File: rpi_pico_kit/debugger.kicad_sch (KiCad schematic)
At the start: 44 parts, among them J3 USB_B, U11 74HC14, U2 RP2040, U3 NCP1117-3.3_SOT223, U4 W25Q16JVSSIQ, Y1 12MHz

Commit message: added MPNs
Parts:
- LED4: Manufacturer Part Number (none) -> LTST-C170KFKT; Supplier (none) -> Digikey; Supplier Part URL (none) -> https://www.digikey.cz/en/products/detail/lite-on-inc/LTST-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
- U3: Manufacturer Part Number (none) -> NCP1117ST33T3G; Supplier (none) -> Digikey; Supplier Part URL (none) -> https://www.digikey.cz/en/products/detail/onsemi/NCP1117ST3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
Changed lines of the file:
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@@
+      (effects (font (size 1.27 1.27)) hide)
+    )
+    (property "Manufacturer Part Number" "NCP1117ST33T3G" (id 4) (at 242.57 40.64 0)
+      (effects (font (size 1.27 1.27)) hide)
+    )
+    (property "Supplier" "Digikey" (id 5) (at 242.57 40.64 0)
+      (effects (font (size 1.27 1.27)) hide)
+    )
+    (property "Supplier Part URL" "https://www.digikey.cz/en/products/detail/onsemi/NCP1117ST33T3G/1749063" (id 6) (at 242.57 40.64 0)
       (effects (font (size 1.27 1.27)) hide)
     )
@@
       (effects (font (size 1.27 1.27)) hide)
     )
+    (property "Manufacturer Part Number" "LTST-C170KFKT" (id 4) (at 265.43 142.24 0)
+      (effects (font (size 1.27 1.27)) hide)
+    )
+    (property "Supplier" "Digikey" (id 5) (at 265.43 142.24 0)
+      (effects (font (size 1.27 1.27)) hide)
+    )
+    (property "Supplier Part URL" "https://www.digikey.cz/en/products/detail/lite-on-inc/LTST-C170KFKT/386775" (id 6) (at 265.43 142.24 0)
+      (effects (font (size 1.27 1.27)) hide)
+    )

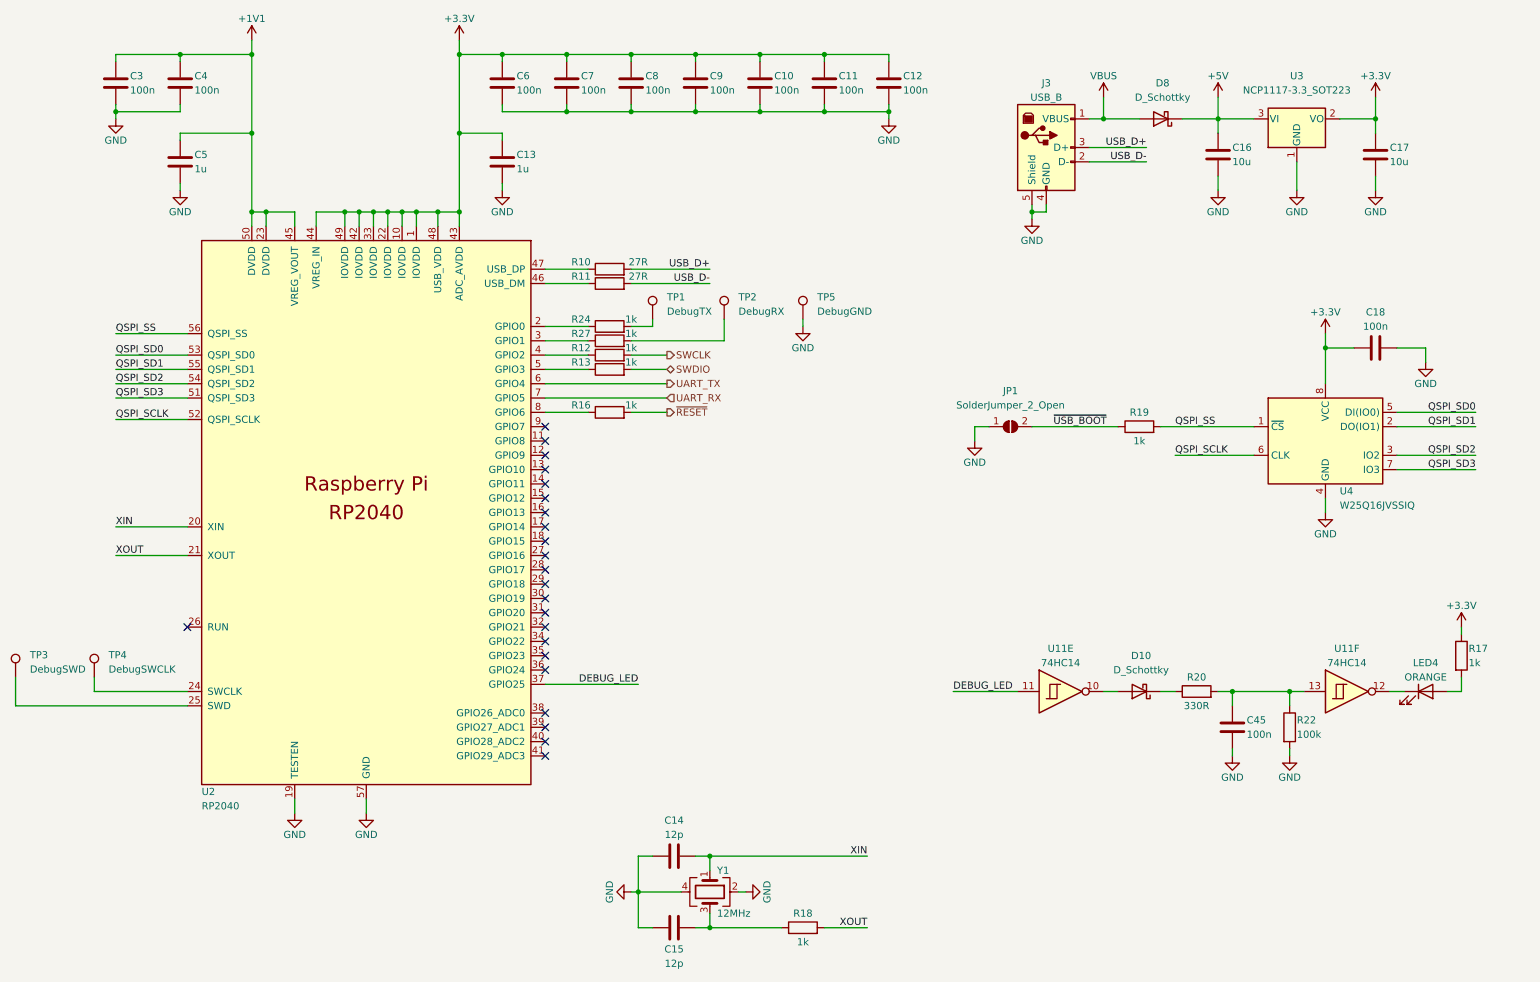
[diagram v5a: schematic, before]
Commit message: changed numbering of parts
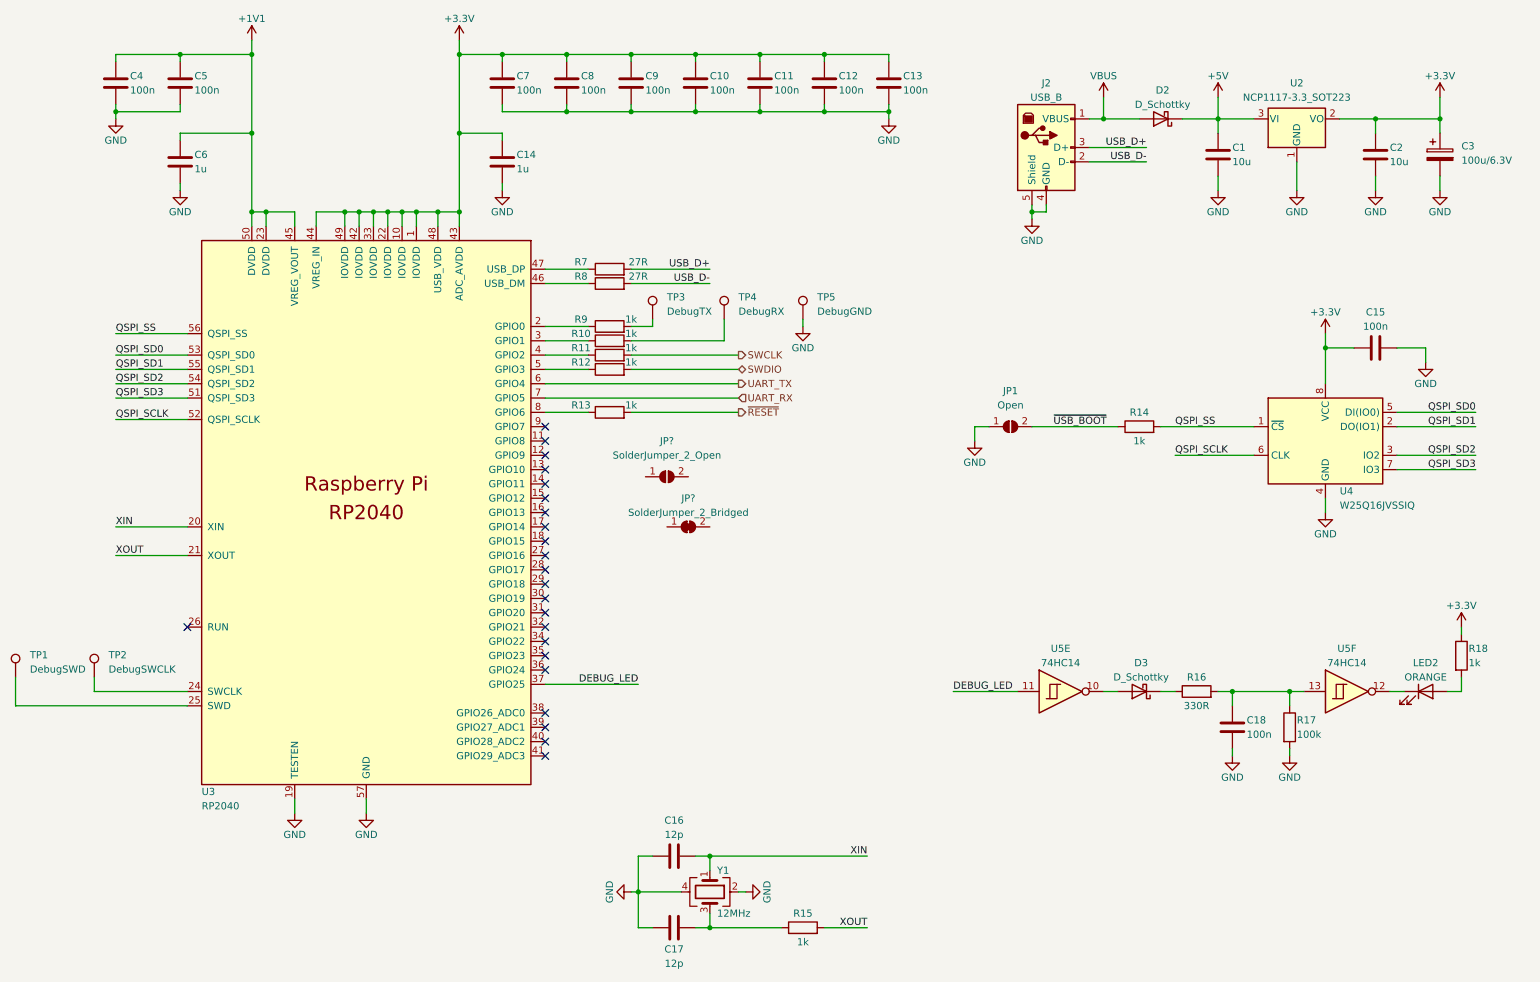
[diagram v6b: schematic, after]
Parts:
- added C3: 100u/6.3V, Capacitor_SMD:C_Elec_6.3x5.4, symbol Device:C_Polarized
- added JP?: SolderJumper_2_Bridged, symbol Jumper:SolderJumper_2_Bridged
- added JP?: SolderJumper_2_Open, Jumper:SolderJumper-2_P1.3mm_Open_RoundedPad1.0x1.5mm, symbol Jumper:SolderJumper_2_Open
- JP1: value SolderJumper_2_Open -> Open
- renumbered C16 to C1, C9 to C10, C10 to C11, C11 to C12, C12 to C13, C13 to C14, C18 to C15, C14 to C16, C15 to C17, C45 to C18, C17 to C2, C3 to C4, C4 to C5, C5 to C6, C6 to C7, C7 to C8, C8 to C9, D8 to D2, D10 to D3, J3 to J2, LED4 to LED2, R27 to R10, R12 to R11, R13 to R12, R16 to R13, R19 to R14, R18 to R15, R20 to R16, R22 to R17, R17 to R18, R10 to R7, R11 to R8, R24 to R9, TP3 to TP1, TP4 to TP2, TP1 to TP3, TP2 to TP4, U3 to U2, U2 to U3, U11 to U5
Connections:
- net +3V3: now also C3.1
- net GND: now also C3.2

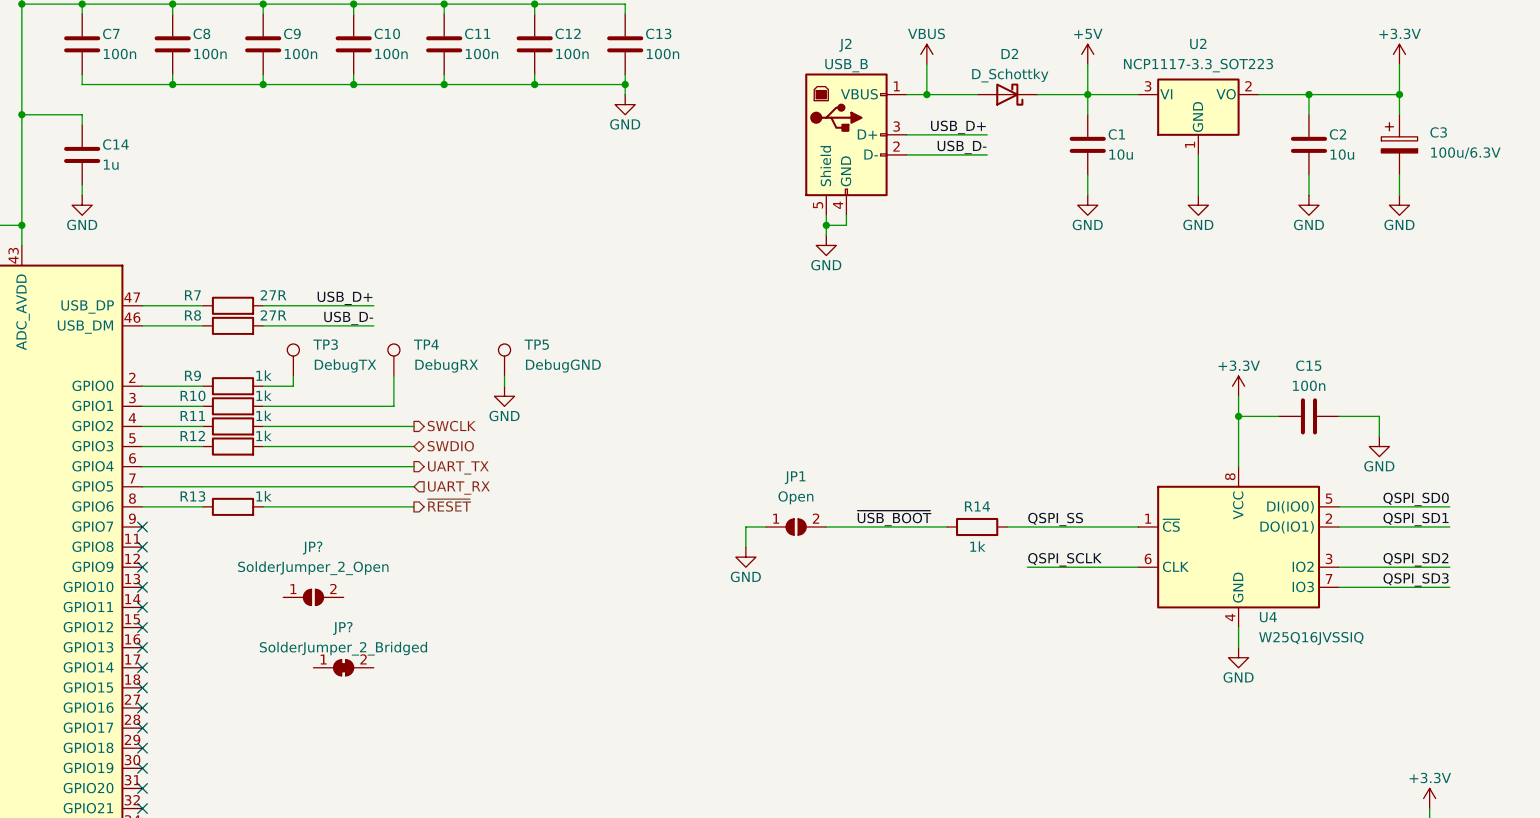
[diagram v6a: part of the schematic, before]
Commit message: added solder jumpers to swd, changed numbering of parts
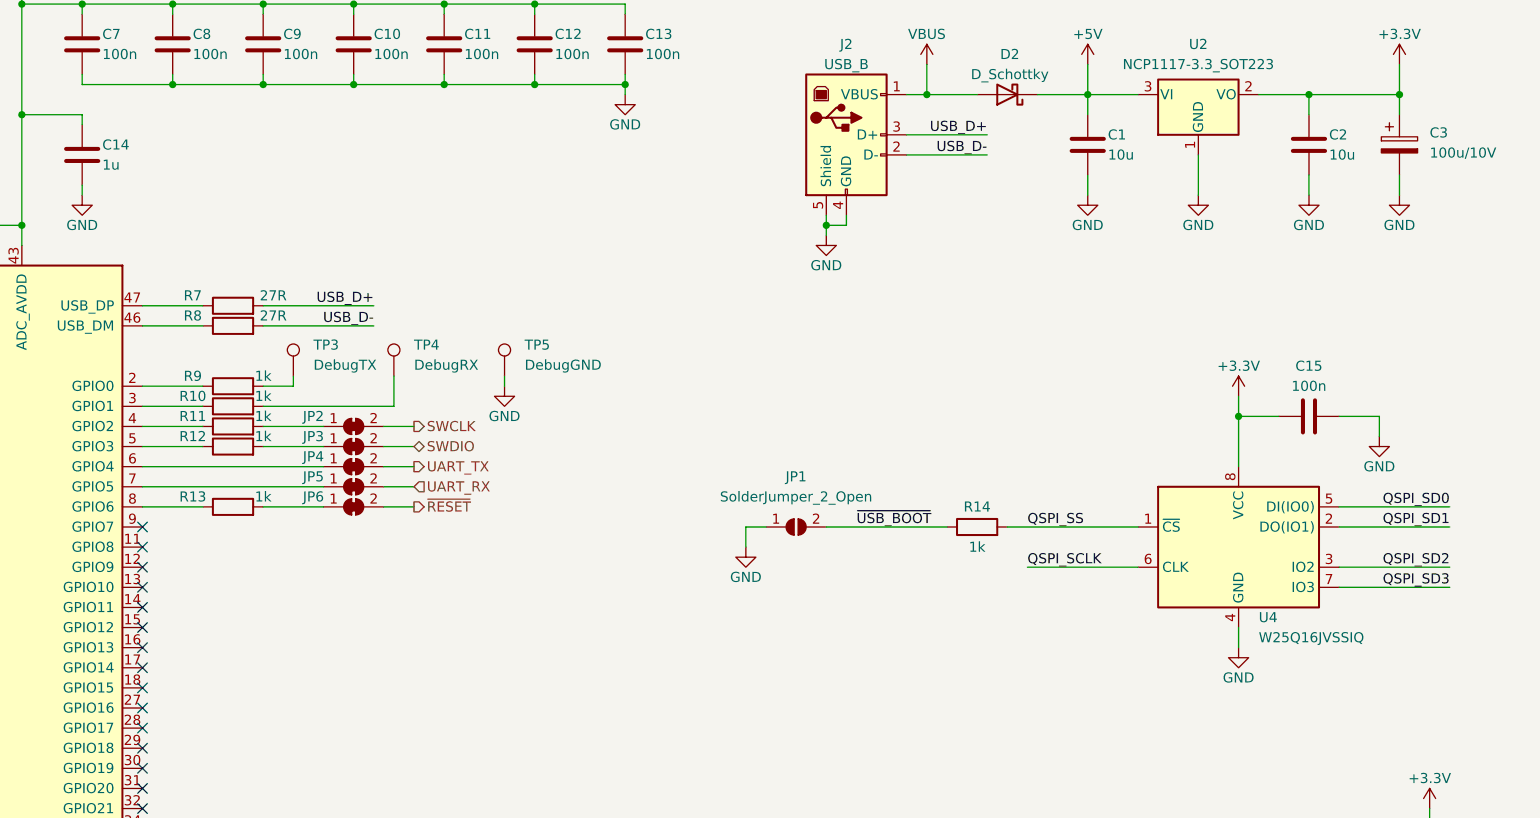
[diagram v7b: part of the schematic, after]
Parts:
- removed JP?: SolderJumper_2_Open, Jumper:SolderJumper-2_P1.3mm_Open_RoundedPad1.0x1.5mm, symbol Jumper:SolderJumper_2_Open
- added JP3, JP4, JP5, JP6: SolderJumper_2_Bridged, Jumper:SolderJumper-2_P1.3mm_Bridged_RoundedPad1.0x1.5mm, symbol Jumper:SolderJumper_2_Bridged
- C3: value 100u/6.3V -> 100u/10V; footprint Capacitor_SMD:C_Elec_6.3x5.4 -> Capacitor_SMD:C_Elec_5x5.4; Manufacturer Part Number 865230143004 -> UWR1A101MCL1GB; Supplier Part URL https://www.digikey.cz/en/products/detail/würth-elektronik/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 -> https://www.digikey.cz/en/products/detail/nichicon/UWR1A101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
- JP1: value Open -> SolderJumper_2_Open
- JP2: renamed from JP?; footprint (none) -> Jumper:SolderJumper-2_P1.3mm_Bridged_RoundedPad1.0x1.5mm
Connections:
- net SWCLK: now also JP2.2 (B); no longer R11.2
- net SWDIO: now also JP3.2 (B); no longer R12.2
- net UART_RX: now also JP5.2 (B); no longer U3.7 (GPIO5)
- net UART_TX: now also JP4.2 (B); no longer U3.6 (GPIO4)
- net ~{RESET}: now also JP6.2 (B); no longer R13.2
- net at JP2.1 (A): now also R11.2
- new net: JP4.1 (A), U3.6 (GPIO4)
- new net: JP5.1 (A), U3.7 (GPIO5)
- new net: JP6.1 (A), R13.2
- new net: JP3.1 (A), R12.2
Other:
- moved on the sheet: JP2

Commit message: little changes
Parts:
- D2, D3: value D_Schottky -> STPS1L30U
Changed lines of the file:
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@@
       (effects (font (size 1.27 1.27)))
     )
-    (property "Value" "D_Schottky" (id 1) (at 218.7575 38.1 0)
+    (property "Value" "STPS1L30U" (id 1) (at 218.7575 38.1 0)
       (effects (font (size 1.27 1.27)))
     )
@@
       (effects (font (size 1.27 1.27)))
     )
-    (property "Value" "D_Schottky" (id 1) (at 214.9475 139.7 0)
-      (effects (font (size 1.27 1.27)))
-    )
+    (property "Value" "STPS1L30U" (id 1) (at 214.9475 139.7 0)
+      (effects (font (size 1.27 1.27)))
+    )
